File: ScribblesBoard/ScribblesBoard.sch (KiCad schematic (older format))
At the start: 22 parts, among them J1 ICSP, J2 Conn_01x04, U1 MIC5205-3.3, U2 ATMEGA328P-MU, U3 BNO055

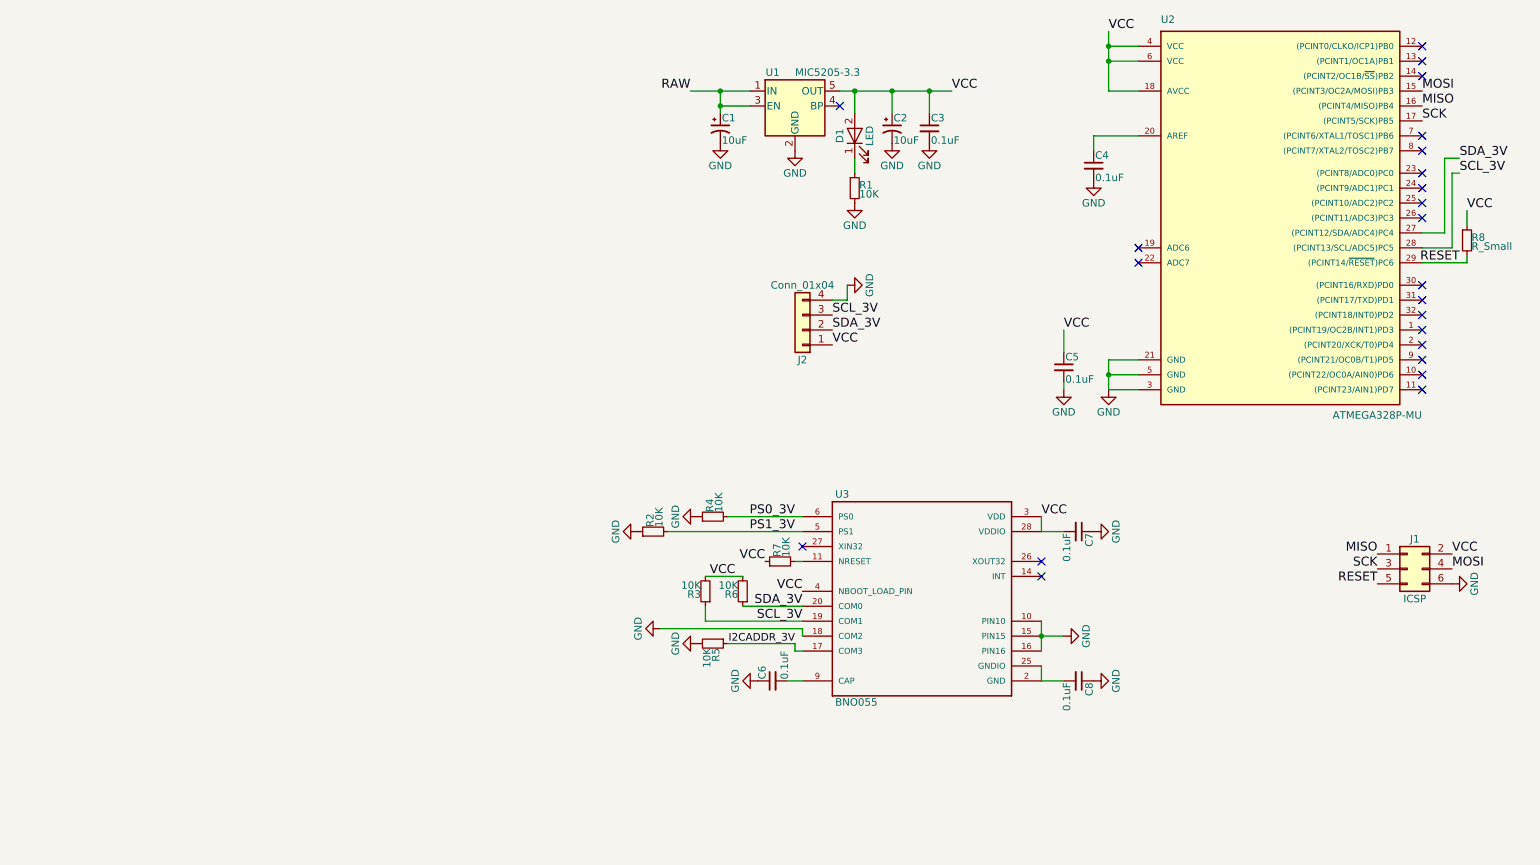
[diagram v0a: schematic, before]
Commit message: Finished bluetooth board
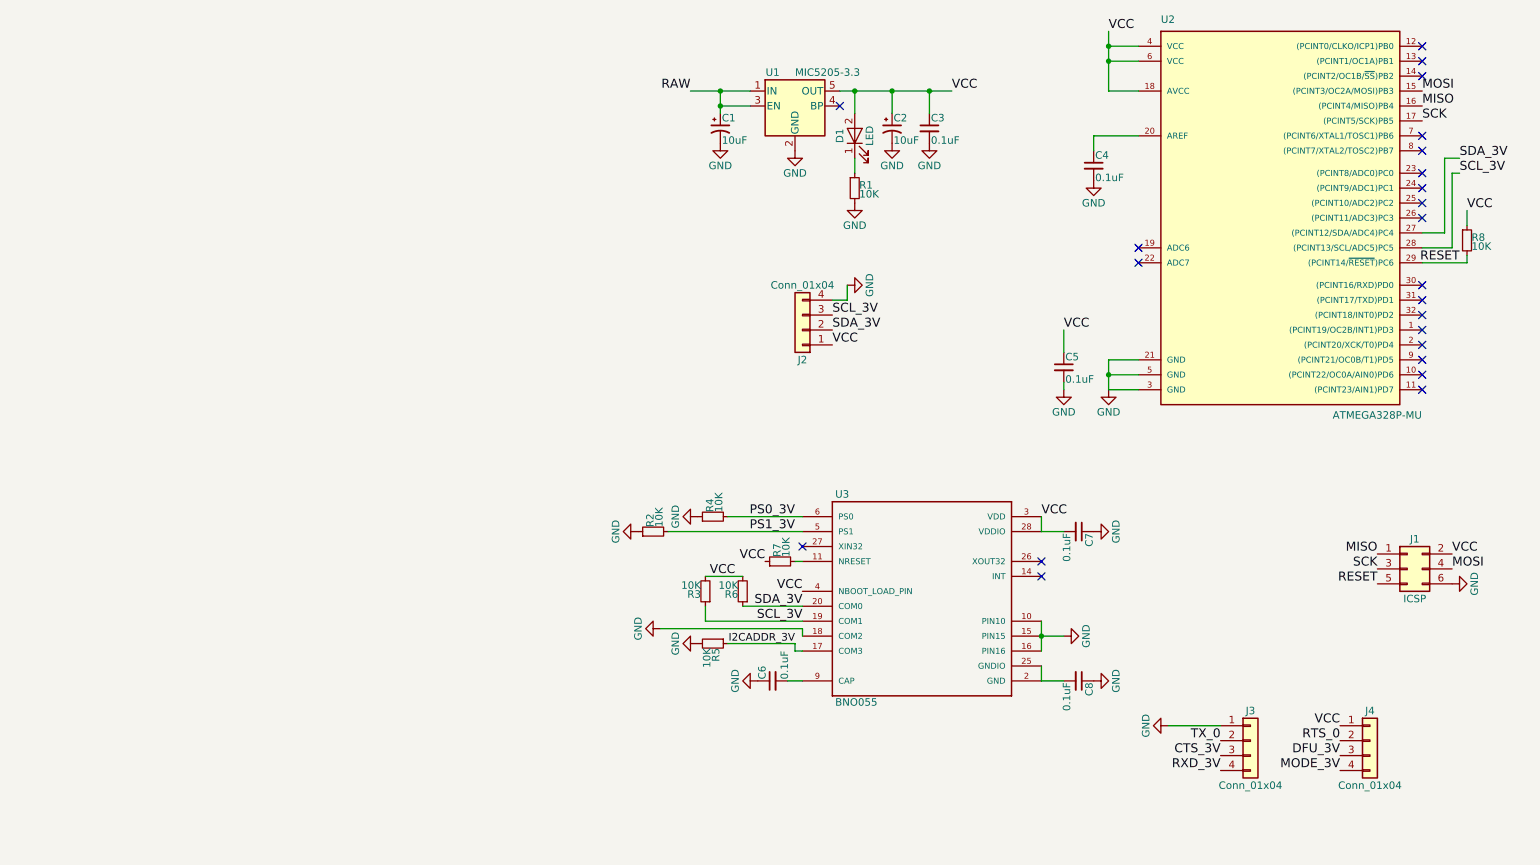
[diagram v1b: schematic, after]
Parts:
- added J3, J4: Conn_01x04, Pin_Headers:Pin_Header_Straight_1x04_Pitch2.54mm, symbol Conn_01x04
- R8: value R_Small -> 10K
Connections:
- net GND: now also J3.1 (Pin_1)
- net VCC: now also J4.1 (Pin_1)
- new net CTS_3V: J3.3 (Pin_3)
- new net DFU_3V: J4.3 (Pin_3)
- new net MODE_3V: J4.4 (Pin_4)
- new net RTS_0: J4.2 (Pin_2)
- new net RXD_3V: J3.4 (Pin_4)
- new net TX_0: J3.2 (Pin_2)
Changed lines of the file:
@@
 NoConn ~ 6200 1400
 $Comp
-L GND #PWR01
+L GND #PWR7
 U 1 1 5A7B50B6
 P 5900 1700
-F 0 "#PWR01" H 5900 1450 50  0001 C CNN
+F 0 "#PWR7" H 5900 1450 50  0001 C CNN
 F 1 "GND" H 5900 1550 50  0000 C CNN
 F 2 "" H 5900 1700 50  0001 C CNN
@@
 $EndComp
 $Comp
-L GND #PWR02
+L GND #PWR17
 U 1 1 5A7B51E2
 P 8000 3300
-F 0 "#PWR02" H 8000 3050 50  0001 C CNN
+F 0 "#PWR17" H 8000 3050 50  0001 C CNN
 F 1 "GND" H 8000 3150 50  0000 C CNN
 F 2 "" H 8000 3300 50  0001 C CNN
@@
 $EndComp
 $Comp
-L GND #PWR03
+L GND #PWR5
 U 1 1 5A7B53E3
 P 5400 1650
-F 0 "#PWR03" H 5400 1400 50  0001 C CNN
+F 0 "#PWR5" H 5400 1400 50  0001 C CNN
 F 1 "GND" H 5400 1500 50  0000 C CNN
 F 2 "" H 5400 1650 50  0001 C CNN
@@
 VCC
 $Comp
-L GND #PWR04
+L GND #PWR10
 U 1 1 5A7B56D2
 P 6550 1650
-F 0 "#PWR04" H 6550 1400 50  0001 C CNN
+F 0 "#PWR10" H 6550 1400 50  0001 C CNN
 F 1 "GND" H 6550 1500 50  0000 C CNN
 F 2 "" H 6550 1650 50  0001 C CNN
@@
 $EndComp
 $Comp
-L GND #PWR05
+L GND #PWR11
 U 1 1 5A7B56F0
 P 6800 1650
-F 0 "#PWR05" H 6800 1400 50  0001 C CNN
+F 0 "#PWR11" H 6800 1400 50  0001 C CNN
 F 1 "GND" H 6800 1500 50  0000 C CNN
 F 2 "" H 6800 1650 50  0001 C CNN
@@
 $EndComp
 $Comp
-L GND #PWR06
+L GND #PWR9
 U 1 1 5A7B59E6
 P 6300 2050
-F 0 "#PWR06" H 6300 1800 50  0001 C CNN
+F 0 "#PWR9" H 6300 1800 50  0001 C CNN
 F 1 "GND" H 6300 1900 50  0000 C CNN
 F 2 "" H 6300 2050 50  0001 C CNN
@@
 $EndComp
 $Comp
-L GND #PWR07
+L GND #PWR14
 U 1 1 5A7B5B6B
 P 7900 1900
-F 0 "#PWR07" H 7900 1650 50  0001 C CNN
+F 0 "#PWR14" H 7900 1650 50  0001 C CNN
 F 1 "GND" H 7900 1750 50  0000 C CNN
 F 2 "" H 7900 1900 50  0001 C CNN
@@
 VCC
 $Comp
-L GND #PWR08
+L GND #PWR12
 U 1 1 5A7B5DFD
 P 7700 3300
-F 0 "#PWR08" H 7700 3050 50  0001 C CNN
+F 0 "#PWR12" H 7700 3050 50  0001 C CNN
 F 1 "GND" H 7700 3150 50  0000 C CNN
 F 2 "" H 7700 3300 50  0001 C CNN
@@
 $EndComp
 $Comp
-L GND #PWR09
+L GND #PWR15
 U 1 1 5A80C723
 P 7900 4250
-F 0 "#PWR09" H 7900 4000 50  0001 C CNN
+F 0 "#PWR15" H 7900 4000 50  0001 C CNN
 F 1 "GND" H 7900 4100 50  0000 C CNN
 F 2 "" H 7900 4250 50  0001 C CNN
@@
 $EndComp
 $Comp
-L GND #PWR010
+L GND #PWR16
 U 1 1 5A80C9A6
 P 7900 5250
-F 0 "#PWR010" H 7900 5000 50  0001 C CNN
+F 0 "#PWR16" H 7900 5000 50  0001 C CNN
 F 1 "GND" H 7900 5100 50  0000 C CNN
 F 2 "" H 7900 5250 50  0001 C CNN
@@
 $EndComp
 $Comp
-L GND #PWR011
+L GND #PWR6
 U 1 1 5A80CBA1
 P 5650 5250
-F 0 "#PWR011" H 5650 5000 50  0001 C CNN
+F 0 "#PWR6" H 5650 5000 50  0001 C CNN
 F 1 "GND" H 5650 5100 50  0000 C CNN
 F 2 "" H 5650 5250 50  0001 C CNN
@@
 $EndComp
 $Comp
-L GND #PWR012
+L GND #PWR13
 U 1 1 5A80CE46
 P 7700 4950
-F 0 "#PWR012" H 7700 4700 50  0001 C CNN
+F 0 "#PWR13" H 7700 4700 50  0001 C CNN
 F 1 "GND" H 7700 4800 50  0000 C CNN
 F 2 "" H 7700 4950 50  0001 C CNN
@@
 $EndComp
 $Comp
-L GND #PWR013
+L GND #PWR4
 U 1 1 5A80D56F
 P 5250 5000
-F 0 "#PWR013" H 5250 4750 50  0001 C CNN
+F 0 "#PWR4" H 5250 4750 50  0001 C CNN
 F 1 "GND" H 5250 4850 50  0000 C CNN
 F 2 "" H 5250 5000 50  0001 C CNN
@@
 $EndComp
 $Comp
-L GND #PWR014
+L GND #PWR3
 U 1 1 5A80DB44
 P 5250 4150
-F 0 "#PWR014" H 5250 3900 50  0001 C CNN
+F 0 "#PWR3" H 5250 3900 50  0001 C CNN
 F 1 "GND" H 5250 4000 50  0000 C CNN
 F 2 "" H 5250 4150 50  0001 C CNN
@@
 $EndComp
 $Comp
-L GND #PWR015
+L GND #PWR1
 U 1 1 5A80DC63
 P 4850 4250
-F 0 "#PWR015" H 4850 4000 50  0001 C CNN
+F 0 "#PWR1" H 4850 4000 50  0001 C CNN
 F 1 "GND" H 4850 4100 50  0000 C CNN
 F 2 "" H 4850 4250 50  0001 C CNN
@@
 SCL_3V
 $Comp
-L GND #PWR016
+L GND #PWR2
 U 1 1 5A80E850
 P 5000 4900
-F 0 "#PWR016" H 5000 4650 50  0001 C CNN
+F 0 "#PWR2" H 5000 4650 50  0001 C CNN
 F 1 "GND" H 5000 4750 50  0000 C CNN
 F 2 "" H 5000 4900 50  0001 C CNN
@@
 MOSI
 $Comp
-L GND #PWR017
+L GND #PWR19
 U 1 1 5A8E180E
 P 10300 4600
-F 0 "#PWR017" H 10300 4350 50  0001 C CNN
+F 0 "#PWR19" H 10300 4350 50  0001 C CNN
 F 1 "GND" H 10300 4450 50  0000 C CNN
 F 2 "" H 10300 4600 50  0001 C CNN
@@
 P 10400 2300
 F 0 "R8" H 10430 2320 50  0000 L CNN
-F 1 "R_Small" H 10430 2260 50  0000 L CNN
+F 1 "10K" H 10430 2260 50  0000 L CNN
 F 2 "Resistors_SMD:R_0201" H 10400 2300 50  0001 C CNN
 F 3 "" H 10400 2300 50  0001 C CNN
@@
 VCC
 $Comp
-L GND #PWR018
+L GND #PWR8
 U 1 1 5A8E5E13
 P 6250 2600
-F 0 "#PWR018" H 6250 2350 50  0001 C CNN
+F 0 "#PWR8" H 6250 2350 50  0001 C CNN
 F 1 "GND" H 6250 2450 50  0000 C CNN
 F 2 "" H 6250 2600 50  0001 C CNN
@@
 	5200 1300 5600 1300
 Wire Wire Line
-	5400 1450 5400 1300
+	5400 1300 5400 1450
 Connection ~ 5400 1300
 Wire Wire Line
@@
 	8000 1300 8200 1300
 Wire Wire Line
-	8200 1100 8000 1100
+	8000 1100 8200 1100
 Connection ~ 8000 1100
 Wire Wire Line
@@
 Wire Wire Line
 	8000 900  8000 1300
+$Comp
+L Conn_01x04 J3
+U 1 1 5A98E0AF
+P 8950 5650
+F 0 "J3" H 8950 5850 50  0000 C CNN
+F 1 "Conn_01x04" H 8950 5350 50  0000 C CNN
+F 2 "Pin_Headers:Pin_Header_Straight_1x04_Pitch2.54mm" H 8950 5650 50  0001 C CNN
+F 3 "" H 8950 5650 50  0001 C CNN
+	1    8950 5650
+	1    0    0    -1
+$EndComp
+$Comp
+L Conn_01x04 J4
+U 1 1 5A98E14F
+P 9750 5650
+F 0 "J4" H 9750 5850 50  0000 C CNN
+F 1 "Conn_01x04" H 9750 5350 50  0000 C CNN
+F 2 "Pin_Headers:Pin_Header_Straight_1x04_Pitch2.54mm" H 9750 5650 50  0001 C CNN
+F 3 "" H 9750 5650 50  0001 C CNN
+	1    9750 5650
+	1    0    0    -1
+$EndComp
+$Comp
+L GND #PWR18
+U 1 1 5A98EB85
+P 8400 5550
+F 0 "#PWR18" H 8400 5300 50  0001 C CNN
+F 1 "GND" H 8400 5400 50  0000 C CNN
+F 2 "" H 8400 5550 50  0001 C CNN
+F 3 "" H 8400 5550 50  0001 C CNN
+	1    8400 5550
+	0    1    1    0
+$EndComp
+Text Label 8750 5650 2    60   ~ 0
+TX_0
+Wire Wire Line
+	8750 5550 8400 5550
+Text Label 8750 5750 2    60   ~ 0
+CTS_3V
+Text Label 8750 5850 2    60   ~ 0
+RXD_3V
+Text Label 9550 5550 2    60   ~ 0
+VCC
+Text Label 9550 5650 2    60   ~ 0
+RTS_0
+Text Label 9550 5750 2    60   ~ 0
+DFU_3V
+Text Label 9550 5850 2    60   ~ 0
+MODE_3V
 $EndSCHEMATC

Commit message: Board without external oscillator
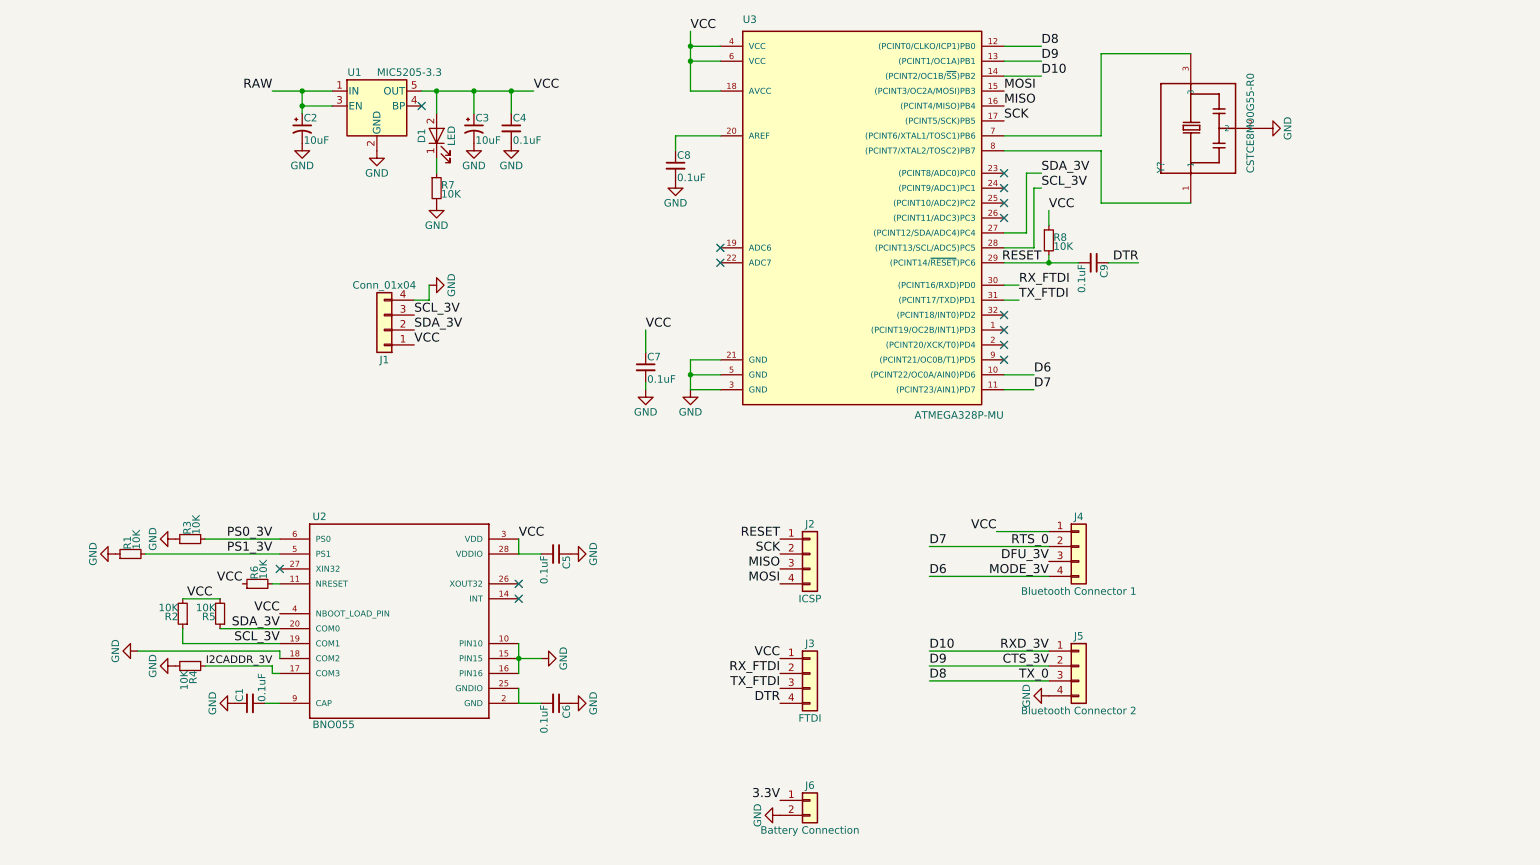
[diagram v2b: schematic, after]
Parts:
- removed J1: ICSP, Pin_Headers:Pin_Header_Straight_2x03_Pitch2.54mm, symbol Conn_02x03_Odd_Even
- added C9: 0.1uF, Capacitors_SMD:C_0402, symbol C_Small
- added J2: ICSP, Pin_Headers:Pin_Header_Straight_1x04_Pitch2.54mm, symbol Conn_01x04
- added J3: FTDI, Pin_Headers:Pin_Header_Straight_1x04_Pitch2.54mm, symbol Conn_01x04
- added J6: Battery Connection, Pin_Headers:Pin_Header_Straight_1x02_Pitch2.54mm, symbol Conn_01x02
- added Y?: CSTCE8M00G55-R0, OSC_CSTCE8M00G55-R0, symbol CSTCE8M00G55-R0
- C1: renamed from C6; footprint Capacitors_SMD:C_0201 -> Capacitors_SMD:C_0402
- C2: renamed from C1; footprint Capacitors_SMD:C_1206 -> Capacitors_SMD:C_0603
- C3: renamed from C2; footprint Capacitors_SMD:C_1206 -> Capacitors_SMD:C_0603
- C4: renamed from C3; footprint Capacitors_SMD:C_0201 -> Capacitors_SMD:C_0402
- C5: renamed from C7; footprint Capacitors_SMD:C_0201 -> Capacitors_SMD:C_0402
- C6: renamed from C8; footprint Capacitors_SMD:C_0201 -> Capacitors_SMD:C_0402
- C7: renamed from C5; footprint Capacitors_SMD:C_0201 -> Capacitors_SMD:C_0402
- C8: renamed from C4; footprint Capacitors_SMD:C_0201 -> Capacitors_SMD:C_0402
- J4: renamed from J3; value Conn_01x04 -> Bluetooth Connector 1
- J5: renamed from J4; value Conn_01x04 -> Bluetooth Connector 2
- R1: renamed from R2; footprint Resistors_SMD:R_0201 -> Resistors_SMD:R_0402
- R2: renamed from R3; footprint Resistors_SMD:R_0201 -> Resistors_SMD:R_0402
- R3: renamed from R4; footprint Resistors_SMD:R_0201 -> Resistors_SMD:R_0402
- R4: renamed from R5; footprint Resistors_SMD:R_0201 -> Resistors_SMD:R_0402
- R5: renamed from R6; footprint Resistors_SMD:R_0201 -> Resistors_SMD:R_0402
- R6: renamed from R7; footprint Resistors_SMD:R_0201 -> Resistors_SMD:R_0402
- R7: renamed from R1; footprint Resistors_SMD:R_0201 -> Resistors_SMD:R_0402
- R8: footprint Resistors_SMD:R_0201 -> Resistors_SMD:R_0402
- renumbered J2 to J1, U3 to U2, U2 to U3
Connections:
- net MODE_3V is gone; now on net GND: J5.4 (Pin_4)
- net RTS_0 is gone; now on net CTS_3V: J5.2 (Pin_2)
- net RXD_3V is gone; now on net D6: J4.4 (Pin_4)
- net TX_0 is gone; now on net D7: J4.2 (Pin_2)
- net CTS_3V: now also U3.13 ((PCINT1/OC1A)PB1); no longer J4.3 (Pin_3)
- net DFU_3V: now also J4.3 (Pin_3); no longer J5.3 (Pin_3)
- net GND: now also J6.2 (Pin_2), Y?.2; no longer J4.1 (Pin_1)
- net MISO: now also J2.3 (Pin_3)
- net MOSI: now also J2.4 (Pin_4)
- net RESET: now also C9.2, J2.1 (Pin_1)
- net SCK: now also J2.2 (Pin_2)
- net VCC: now also J4.1 (Pin_1), J3.1 (Pin_1); no longer J5.1 (Pin_1)
- net D6: now reaches U3.10 ((PCINT22/OC0A/AIN0)PD6)
- net D7: now reaches U3.11 ((PCINT23/AIN1)PD7)
- net D8: now reaches U3.12 ((PCINT0/CLKO/ICP1)PB0)
- net D8: now also J5.3 (Pin_3)
- net D10: now reaches U3.14 ((PCINT2/OC1B/~SS~)PB2)
- net D10: now also J5.1 (Pin_1)
- net RX_FTDI: now reaches U3.30 ((PCINT16/RXD)PD0)
- net RX_FTDI: now also J3.2 (Pin_2)
- net TX_FTDI: now reaches U3.31 ((PCINT17/TXD)PD1)
- net TX_FTDI: now also J3.3 (Pin_3)
- net at U3.7 ((PCINT6/XTAL1/TOSC1)PB6): now also Y?.3
- net at U3.8 ((PCINT7/XTAL2/TOSC2)PB7): now also Y?.1
- new net 3.3V: J6.1 (Pin_1)
- new net DTR: C9.1, J3.4 (Pin_4)
- no-connect marks 23 -> 14
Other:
- moved on the sheet: C1, C2, C3, C4, C5, C6, C7, C8, D1, J1, J4, J5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
